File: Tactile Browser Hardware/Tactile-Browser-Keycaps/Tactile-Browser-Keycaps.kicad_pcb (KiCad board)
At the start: 2 copper layers, 23.5 x 19 mm, 3 parts, among them J1 Conn_01x01_Pin, J2 Conn_01x01_Pin, SW1 SW_Push

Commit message: ketyswitch
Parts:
- removed J2: Conn_01x01_Pin, Connector_PinHeader_2.54mm:PinHeader_1x01_P2.54mm_Horizontal
- J1: value Conn_01x01_Pin -> Conn_01x02_Pin; footprint Connector_PinHeader_2.54mm:PinHeader_1x01_P2.54mm_Horizontal -> Connector_JST:JST_PH_B2B-PH-SM4-TB_1x02-1MP_P2.00mm_Vertical; moved to B.Cu
- moved J1 6.35 mm to (103.8, 101.5), turned to 0 degrees
- moved SW1 0.96 mm to (110.0, 91.3)
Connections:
- SW1 pad 1: Net-(J2-Pin_1) -> Net-(J1-Pin_1)
- SW1 pad 2: Net-(J1-Pin_1) -> Net-(J1-Pin_2)
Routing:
- net Net-(J1-Pin_1): track 0.04 -> 20.6 mm
- net Net-(J1-Pin_2): track 0.00 -> 7.50 mm
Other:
- board size 23.5 x 19 mm -> 15.8 x 17 mm

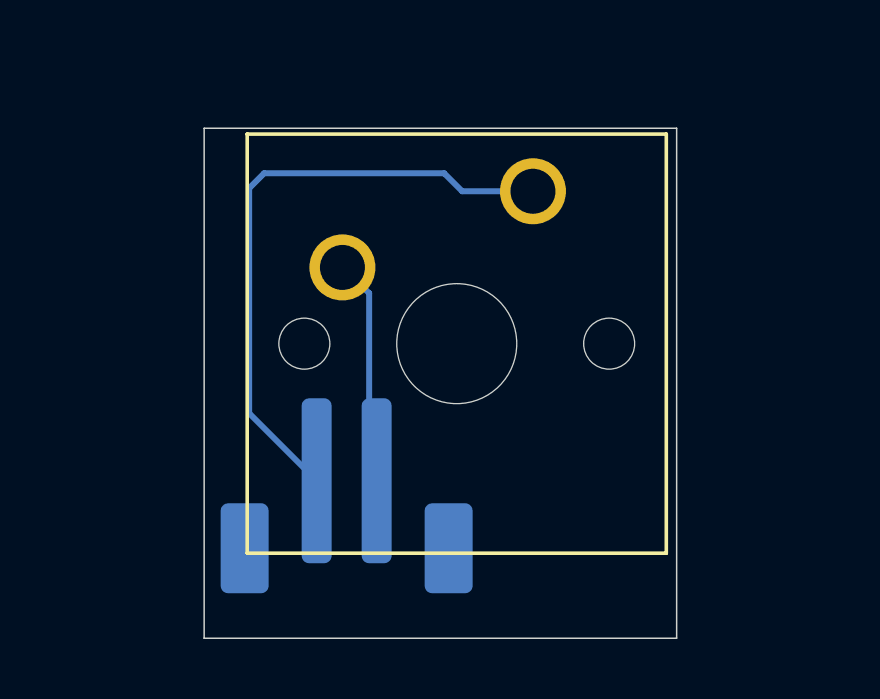
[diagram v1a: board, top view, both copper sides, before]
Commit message: finished keyswitch
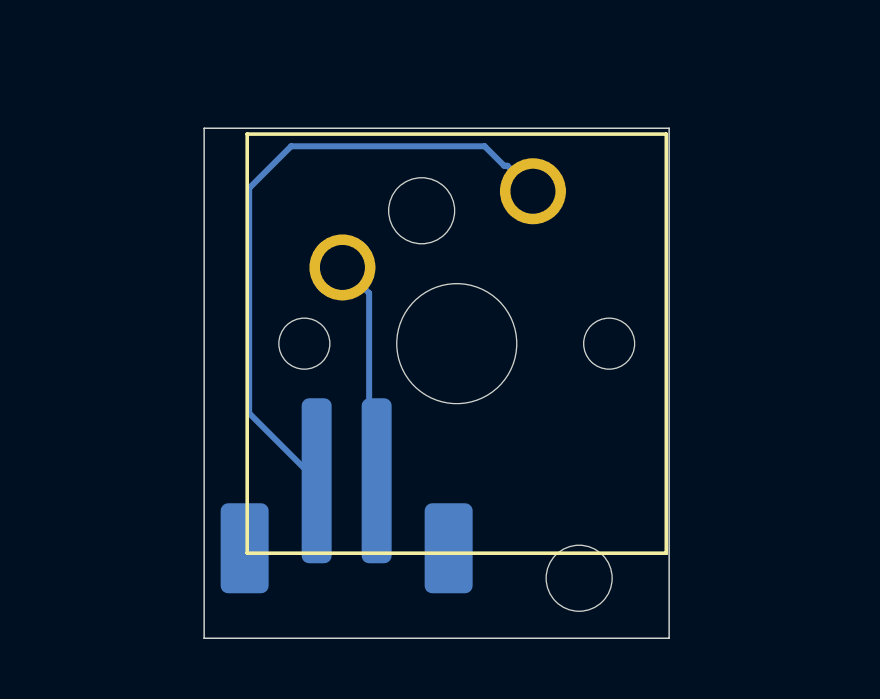
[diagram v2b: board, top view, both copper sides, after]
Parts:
- added REF**: MountingHole_2.2mm_M2, MountingHole:MountingHole_2.2mm_M2, F.Cu at (111.5, 104.2)
- added REF**: MountingHole_2.2mm_M2, MountingHole:MountingHole_2.2mm_M2, F.Cu at (106.2, 92.0)
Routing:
- net Net-(J1-Pin_1): track 20.6 -> 21.3 mm
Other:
- board size 15.8 x 17 mm -> 15.5 x 17 mm
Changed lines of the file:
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@@
 	(net 1 "Net-(J1-Pin_2)")
 	(net 2 "Net-(J1-Pin_1)")
+	(footprint "MountingHole:MountingHole_2.2mm_M2"
+		(layer "F.Cu")
+		(at 111.5 104.25)
+		(descr "Mounting Hole 2.2mm, M2, no annular, generated by kicad-footprint-generator mountinghole.py")
+		(tags "mountinghole M2")
+		(property "Reference" "REF**"
+			(at 0 -3.15 0)
+			(layer "F.SilkS")
+			(hide yes)
+			(effects
+				(font
+					(size 1 1)
+					(thickness 0.15)
+				)
+			)
+		)
+		(property "Value" "MountingHole_2.2mm_M2"
+			(at 0 3.15 0)
+			(layer "F.Fab")
+			(hide yes)
+			(effects
+				(font
+					(size 1 1)
+					(thickness 0.15)
+				)
+			)
+		)
+		(property "Datasheet" ""
+			(at 0 0 0)
+			(layer "F.Fab")
+			(hide yes)
+			(effects
+				(font
+					(size 1.27 1.27)
+					(thickness 0.15)
+				)
+			)
+		)
+		(property "Description" ""
+			(at 0 0 0)
+			(layer "F.Fab")
+			(hide yes)
+			(effects
+				(font
+					(size 1.27 1.27)
+					(thickness 0.15)
+				)
+			)
+		)
+		(attr exclude_from_pos_files exclude_from_bom)
+		(fp_circle
+			(center 0 0)
+			(end 2.2 0)
+			(stroke
+				(width 0.15)
+				(type solid)
+			)
+			(fill no)
+			(layer "Cmts.User")
+		)
+		(fp_circle
+			(center 0 0)
+			(end 2.45 0)
+			(stroke
+				(width 0.05)
+				(type solid)
+			)
+			(fill no)
+			(layer "F.CrtYd")
+		)
+		(pad "" np_thru_hole circle
+			(at 0 0)
+			(size 2.2 2.2)
+			(drill 2.2)
+			(layers "*.Cu" "*.Mask")
+		)
+		(embedded_fonts no)
+	)
+	(footprint "MountingHole:MountingHole_2.2mm_M2"
+		(layer "F.Cu")
+		(at 106.25 92)
+		(descr "Mounting Hole 2.2mm, M2, no annular, generated by kicad-footprint-generator mountinghole.py")
+		(tags "mountinghole M2")
+		(property "Reference" "REF**"
+			(at 0 -3.15 0)
+			(layer "F.SilkS")
+			(hide yes)
+			(effects
+				(font
+					(size 1 1)
+					(thickness 0.15)
+				)
+			)
+		)
+		(property "Value" "MountingHole_2.2mm_M2"
+			(at 0 3.15 0)
+			(layer "F.Fab")
+			(hide yes)
+			(effects
+				(font
+					(size 1 1)
+					(thickness 0.15)
+				)
+			)
+		)
+		(property "Datasheet" ""
+			(at 0 0 0)
+			(layer "F.Fab")
+			(hide yes)
+			(effects
+				(font
+					(size 1.27 1.27)
+					(thickness 0.15)
+				)
+			)
+		)
+		(property "Description" ""
+			(at 0 0 0)
+			(layer "F.Fab")
+			(hide yes)
+			(effects
+				(font
+					(size 1.27 1.27)
+					(thickness 0.15)
+				)
+			)
+		)
+		(attr exclude_from_pos_files exclude_from_bom)
+		(fp_circle
+			(center 0 0)
+			(end 2.2 0)
+			(stroke
+				(width 0.15)
+				(type solid)
+			)
+			(fill no)
+			(layer "Cmts.User")
+		)
+		(fp_circle
+			(center 0 0)
+			(end 2.45 0)
+			(stroke
+				(width 0.05)
+				(type solid)
+			)
+			(fill no)
+			(layer "F.CrtYd")
+		)
+		(pad "" np_thru_hole circle
+			(at 0 0)
+			(size 2.2 2.2)
+			(drill 2.2)
+			(layers "*.Cu" "*.Mask")
+		)
+		(embedded_fonts no)
+	)
 	(footprint "Button_Switch_Keyboard:SW_Cherry_MX_1.00u_PCB"
 		(layer "F.Cu")
@@
 	(gr_rect
 		(start 99 89.25)
-		(end 114.75 106.25)
+		(end 114.5 106.25)
 		(stroke
 			(width 0.05)
@@
 	)
 	(segment
-		(start 107.6 91.35)
-		(end 107 90.75)
-		(width 0.2)
-		(layer "B.Cu")
-		(net 2)
-	)
-	(segment
 		(start 100.5 98.75)
 		(end 102.75 101)
@@
 	)
 	(segment
+		(start 109.96 91.35)
+		(end 109.11 90.5)
+		(width 0.2)
+		(layer "B.Cu")
+		(net 2)
+	)
+	(segment
+		(start 108.351 89.851)
+		(end 101.899 89.851)
+		(width 0.2)
+		(layer "B.Cu")
+		(net 2)
+	)
+	(segment
 		(start 100.5 91.25)
 		(end 100.5 98.75)
@@
 	)
 	(segment
-		(start 101 90.75)
+		(start 109 90.5)
+		(end 108.351 89.851)
+		(width 0.2)
+		(layer "B.Cu")
+		(net 2)
+	)
+	(segment
+		(start 101.899 89.851)
 		(end 100.5 91.25)
 		(width 0.2)
@@
 	)
 	(segment
-		(start 109.96 91.35)
-		(end 107.6 91.35)
-		(width 0.2)
-		(layer "B.Cu")
-		(net 2)
-	)
-	(segment
-		(start 107 90.75)
-		(end 101 90.75)
-		(width 0.2)
-		(layer "B.Cu")
+		(start 109.11 90.5)
+		(end 109 90.5)
+		(width 0.2)
+		(layer "B.Cu")
